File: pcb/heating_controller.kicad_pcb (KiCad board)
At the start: 2 copper layers, 145 x 81 mm, 23 parts

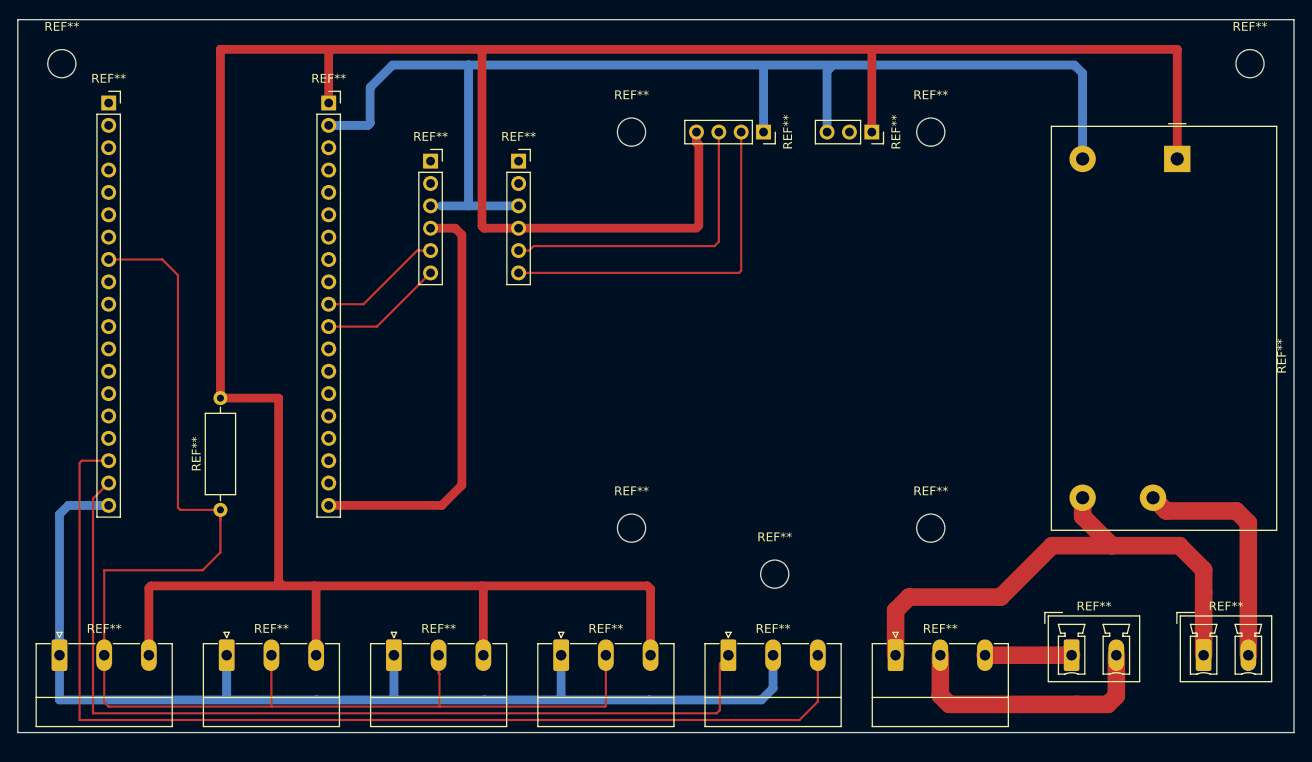
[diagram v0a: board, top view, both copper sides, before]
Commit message: update pcb to fix issues
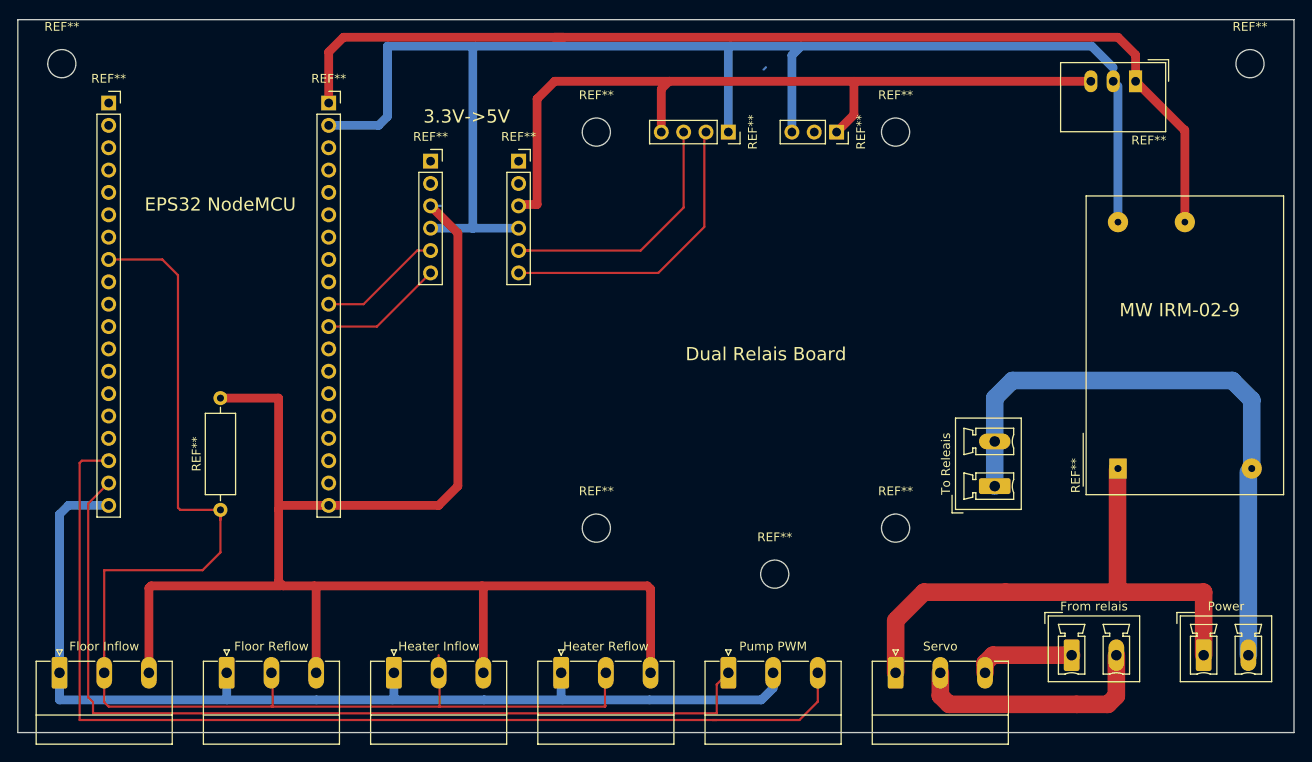
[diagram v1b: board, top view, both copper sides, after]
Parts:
- removed the REF** at (157.7, 83.8)
- added REF**: Converter_ACDC_MeanWell_IRM-02-xx_THT, Converter_ACDC:Converter_ACDC_MeanWell_IRM-02-xx_THT, F.Cu at (151.0, 119.0)
- added REF**: Converter_DCDC_TRACO_TSR-1_THT, Converter_DCDC:Converter_DCDC_TRACO_TSR-1_THT, F.Cu at (153.0, 75.0)
- added To Releais: PhoenixContact_MCV_1,5_2-G-5.08_1x02_P5.08mm_Vertical, Connector_Phoenix_MC_HighVoltage:PhoenixContact_MCV_1,5_2-G-5.08_1x02_P5.08mm_Vertical, F.Cu at (137.0, 121.0)
- Floor Inflow: renamed from REF**
- Floor Reflow: renamed from REF**
- From relais: renamed from REF**
- Heater Inflow: renamed from REF**
- Heater Reflow: renamed from REF**
- Pump PWM: renamed from REF**
- moved REF** 4.00 mm to (91.7, 80.8)
- moved REF** 4.00 mm to (119.0, 80.8)
- moved REF** 4.00 mm to (106.7, 80.8)
- moved REF** 4.00 mm to (91.7, 125.8)
- moved REF** 4.00 mm to (125.7, 80.8)
- moved REF** 4.00 mm to (125.7, 125.8)
- moved Floor Inflow 2.00 mm to (30.7, 142.2)
- moved Floor Reflow 2.00 mm to (49.7, 142.2)
- moved Heater Inflow 2.00 mm to (68.7, 142.2)
- moved Heater Reflow 2.00 mm to (87.7, 142.2)
- moved Pump PWM 2.00 mm to (106.7, 142.2)
- moved Servo 2.00 mm to (125.7, 142.2)
- renumbered REF** to Power, REF** to Servo
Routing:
- net (no net): track 1278.4 -> 1320.0 mm
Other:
- board text added: "3.3V->5V"
- board text added: "Dual Relais Board"
- board text added: "EPS32 NodeMCU"
- board text added: "MW IRM-02-9"
